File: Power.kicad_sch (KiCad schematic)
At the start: 25 parts, among them IC1 NJU7223DL1-33-TE1, J1 USB_C_Receptacle_USB2.0_14P, J2 SM02B-SRSS-TB_LF__SN_, U2 TPS2113APW, U3 MCP73831-2ACI_MC, U4 TPS61093DSKR

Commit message: Create PCB
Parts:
- removed IC1: NJU7223DL1-33-TE1, Footprints:TO-252-3-L1, symbol NJU7223DL1-33-TE1:NJU7223DL1-33-TE1
- removed J1: USB_C_Receptacle_USB2.0_14P, Connector_USB:USB_C_Receptacle_G-Switch_GT-USB-7010ASV, symbol Connector:USB_C_Receptacle_USB2.0_14P
- removed R4: 5.1K, Resistor_SMD:R_0603_1608Metric, symbol Device:R_Small
- removed R6: 200K, Resistor_SMD:R_0603_1608Metric, symbol Device:R_Small
- added C9: 1uF, Capacitor_SMD:C_0603_1608Metric, symbol Device:C_Small
- added J1: 2171790001, Footprints:MOLEX_2171790001, symbol 2171790001:2171790001
- added R2: 5.1K, Resistor_SMD:R_0402_1005Metric, symbol Device:R_Small
- added R7, R8: 100K, Resistor_SMD:R_0402_1005Metric, symbol Device:R_Small
- added U4: TLV1117LV33DCYR, Footprints:VREG_TLV1117LV33DCYR, symbol TLV1117LV33DCYR:TLV1117LV33DCYR
- C10: renamed from C8; footprint Capacitor_SMD:C_0603_1608Metric -> Capacitor_SMD:C_0805_2012Metric; DigiKey_Part_Number (none) -> 1276-1244-1-ND; Manufacturer_Part_Number (none) -> CL21A475KAQNNNE; Price (none) -> €0.30
- C11: renamed from C9; DigiKey_Part_Number (none) -> 311-1445-1-ND; Manufacturer_Part_Number (none) -> CC0603KRX5R8BB105; Price (none) -> €0.95
- C12: renamed from C10; DigiKey_Part_Number (none) -> 311-1341-1-ND; Manufacturer_Part_Number (none) -> CC0603KRX7R8BB104; Price (none) -> €0.48
- C13: renamed from C12; DigiKey_Part_Number (none) -> 311-1341-1-ND; Manufacturer_Part_Number (none) -> CC0603KRX7R8BB104; Price (none) -> €0.48
- C14: renamed from C13; DigiKey_Part_Number (none) -> 311-1445-1-ND; Manufacturer_Part_Number (none) -> CC0603KRX5R8BB105; Price (none) -> €0.95
- C4, C5, C7: DigiKey_Part_Number (none) -> 311-1341-1-ND; Manufacturer_Part_Number (none) -> CC0603KRX7R8BB104; Price (none) -> €0.48
- C6: footprint Capacitor_SMD:C_0603_1608Metric -> Capacitor_SMD:C_0805_2012Metric; DigiKey_Part_Number (none) -> 1276-6455-1-ND; Manufacturer_Part_Number (none) -> CL21A106KOQNNNG; Price (none) -> €0.16
- C8: renamed from C11; footprint Capacitor_SMD:C_0603_1608Metric -> Capacitor_SMD:C_0805_2012Metric; DigiKey_Part_Number (none) -> 1276-6455-1-ND; Manufacturer_Part_Number (none) -> CL21A106KOQNNNG; Price (none) -> €0.16
- J2: AVAILABILITY Good -> (none); Availability In Stock -> (none); Check_prices https://www.snapeda.com/parts/SM02B-SRSS-TB(LF)(SN)/JST/vie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 -> (none); DESCRIPTION SH Series 2 Position 1 mm Pitch Surface Mount Side Entry Sh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 -> (none); Description_1 Connector Header Surface Mount, Right Angle 2 position 0.03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 -> (none); DigiKey_Part_Number (none) -> 455-SM02B-SRSS-TBCT-ND; MF JST Sales -> (none); MP SM02B-SRSS-TB(LF)(SN) -> (none); Manufacturer_Part_Number (none) -> SM02B-SRSS-TB; PACKAGE None -> (none); PRICE 0.23 USD -> (none); Package None -> (none); Price None -> €0.37; SnapEDA_Link https://www.snapeda.com/parts/SM02B-SRSS-TB(LF)(SN)/JST/vie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 -> (none)
- L1: value 10uM -> 10uH; footprint Inductor_SMD:L_0603_1608Metric -> Inductor_SMD:L_0805_2012Metric; DigiKey_Part_Number (none) -> 587-2045-1-ND; Manufacturer_Part_Number (none) -> LBR2012T100K; Price (none) -> €0.10
- R10: renamed from R9; value 10.2K -> 10K; footprint Resistor_SMD:R_0603_1608Metric -> Resistor_SMD:R_0402_1005Metric; DigiKey_Part_Number (none) -> 311-10KJRCT-ND; Manufacturer_Part_Number (none) -> RC0402JR-0710KL; Price (none) -> €0.30
- R3: renamed from R2; value 10k -> 10K; footprint Resistor_SMD:R_0603_1608Metric -> Resistor_SMD:R_0402_1005Metric; DigiKey_Part_Number (none) -> 311-10KJRCT-ND; Manufacturer_Part_Number (none) -> RC0402JR-0710KL; Price (none) -> €0.30
- R4: renamed from R3; value 1k -> 1K; footprint Resistor_SMD:R_0603_1608Metric -> Resistor_SMD:R_1206_3216Metric; DigiKey_Part_Number (none) -> RNCP1206FTD1K00CT-ND; Manufacturer_Part_Number (none) -> RNCP1206FTD1K00; Price (none) -> €0.70
- R5: footprint Resistor_SMD:R_0603_1608Metric -> Resistor_SMD:R_0402_1005Metric; DigiKey_Part_Number (none) -> P5.1KDCCT-ND; Manufacturer_Part_Number (none) -> ERA-2AEB512X; Price (none) -> €0.20
- R6: renamed from R7; value 2k -> 2.7K; footprint Resistor_SMD:R_0603_1608Metric -> Resistor_SMD:R_1206_3216Metric; DigiKey_Part_Number (none) -> 311-2.70KFRCT-ND; Manufacturer_Part_Number (none) -> RC1206FR-072K7L; Price (none) -> €0.10
- R9: renamed from R8; value 294K -> 330K; footprint Resistor_SMD:R_0603_1608Metric -> Resistor_SMD:R_1206_3216Metric; DigiKey_Part_Number (none) -> A129840CT-ND; Manufacturer_Part_Number (none) -> CRGCQ1206F330K; Price (none) -> €0.10
- U2: Availability In Stock -> (none); Check_prices https://www.snapeda.com/parts/TPS2113APW/Texas+Instruments/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 -> (none); Description_1 2.8-V to 5.5-V, 84-mΩ, 1.25-A, power mux with automatic swi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 -> (none); DigiKey_Part_Number (none) -> 296-34596-5-ND; MF Texas Instruments -> (none); MP TPS2113APW -> (none); Manufacturer_Part_Number (none) -> TPS2113APW; Package TSSOP-8 Texas Instruments -> (none); Price None -> €2.61; SnapEDA_Link https://www.snapeda.com/parts/TPS2113APW/Texas+Instruments/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 -> (none)
- U3: Availability In Stock -> (none); Check_prices https://www.snapeda.com/parts/MCP73831-2ACI/MC/Microchip/vi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 -> (none); Description_1 Charge Controller Li-Ion/Li-Pol 15mA to 500mA 4.2V 8-Pin DF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 -> (none); DigiKey_Part_Number (none) -> MCP73831-2ACI/MC-ND; MANUFACTURER MICROCHIP -> (none); MF Microchip -> (none); MP MCP73831-2ACI/MC -> (none); Manufacturer_Part_Number (none) -> MCP73831-2ACI/MC; PARTREV G -> (none); Package VFDFN-8 Microchip -> (none); Price None -> €0.75; STANDARD IPC 7351B -> (none); SnapEDA_Link https://www.snapeda.com/parts/MCP73831-2ACI/MC/Microchip/vi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 -> (none)
- U5: renamed from U4; Availability In Stock -> (none); Check_prices https://www.snapeda.com/parts/TPS61093DSKR/Texas+Instrument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 -> (none); Description_1 Low Input, 20V/1.1A Step-Up DC/DC Converter with Integrated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 -> (none); DigiKey_Part_Number (none) -> 296-39430-1-ND; MF Texas Instruments -> (none); MP TPS61093DSKR -> (none); Manufacturer_Part_Number (none) -> TPS61093DSKR; Package WSON-10 Texas Instruments -> (none); Price None -> €1.96; SnapEDA_Link https://www.snapeda.com/parts/TPS61093DSKR/Texas+Instrument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 -> (none)
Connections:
- net 3V3: now also C9.2
- net GND: now also R5.1, J1.A1B12 (GND1), J1.B1A12 (GND2), J1.SH1 (SHIELD1), J1.SH2 (SHIELD2), J1.SH3 (SHIELD3), J1.SH4 (SHIELD4), R2.2, R8.1, U4.1 (GND); no longer R5.2
- net USB_5V: now also J1.A4B9 (VBUS1), J1.B4A9 (VBUS2)
- net at C11.2, U5.6 (SS): now also R7.2
- net at U2.7 (OUT): now also U4.3 (IN)
- net 15V renamed 17V
- new net: R7.1, R8.2
- new net: C9.1, U4.2 (OUT_2)
- new net: J1.A5 (CC1), R2.1
- new net: J1.B5 (CC2), R5.2
- new net USB_N: J1.A7 (DN1), J1.B7 (DN2)
- new net USB_P: J1.A6 (DP1), J1.B6 (DP2)
- no-connect marks 3 -> 6
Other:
- moved on the sheet: C10, C11, C12, C13, C14, C5, J2, L1, R10, R9, U5

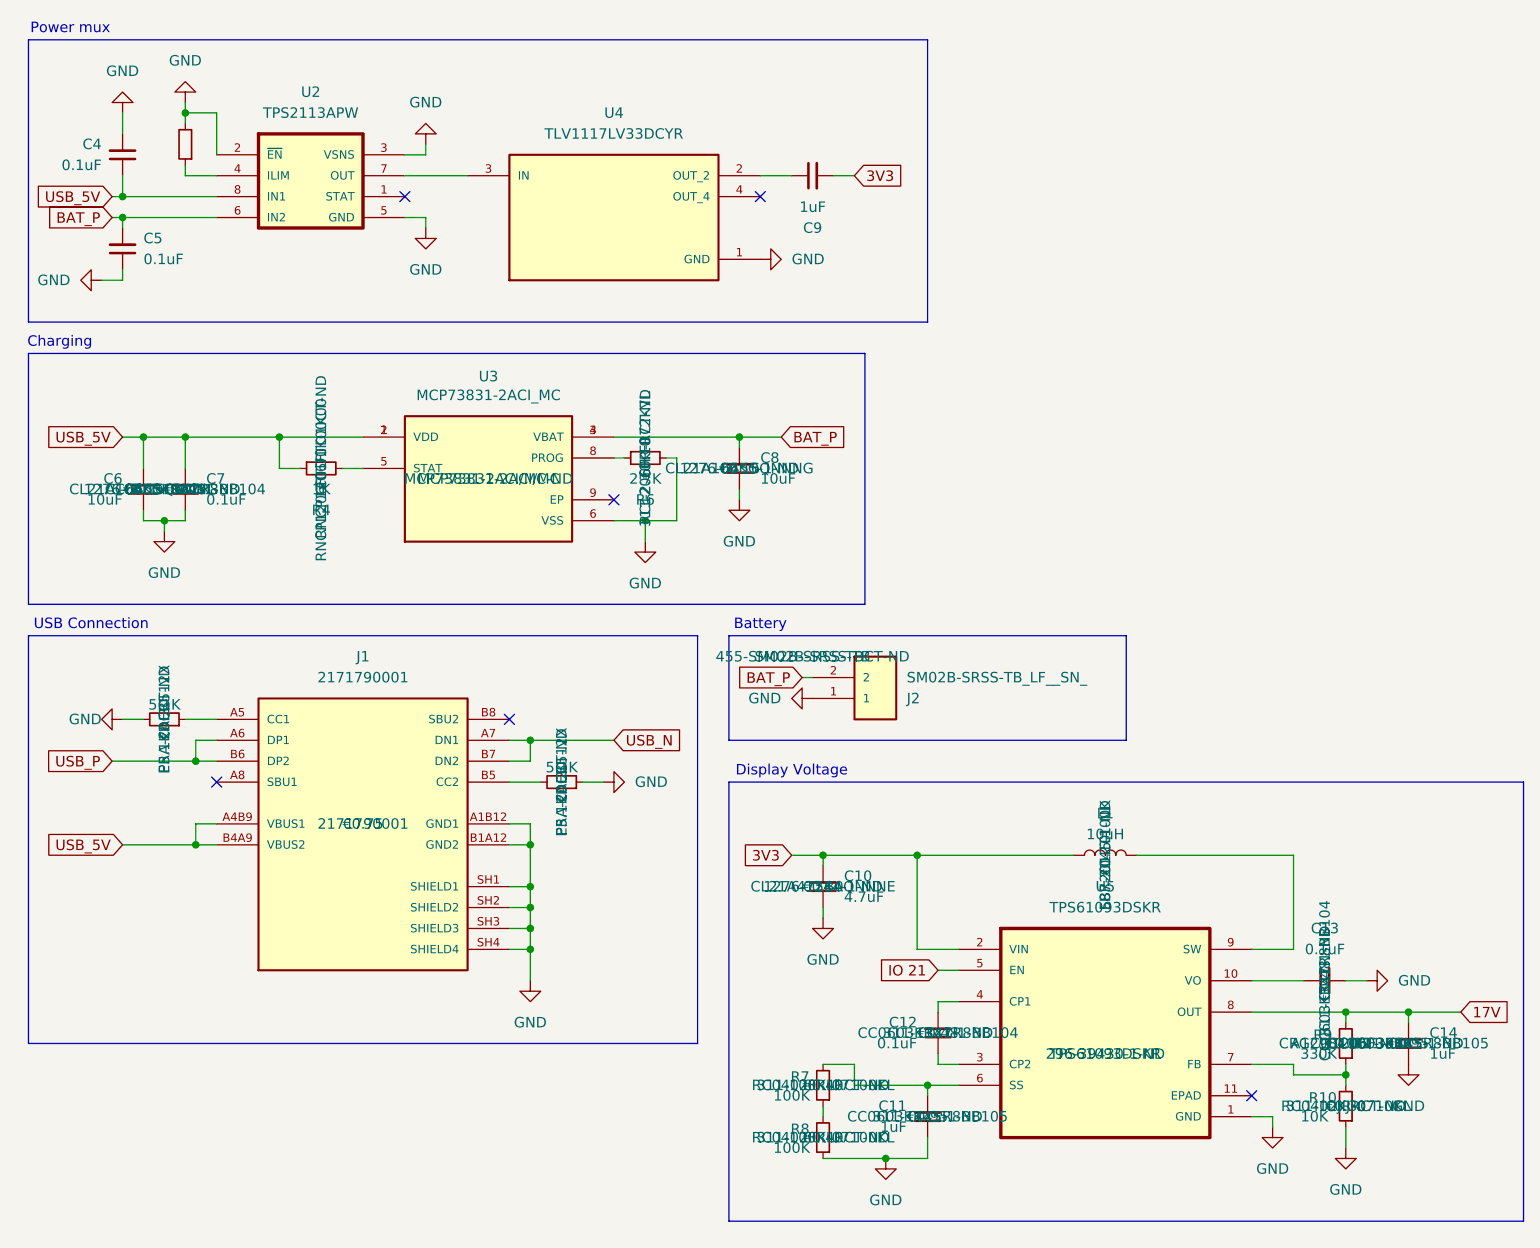
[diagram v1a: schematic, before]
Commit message: Fix minor design mistakes
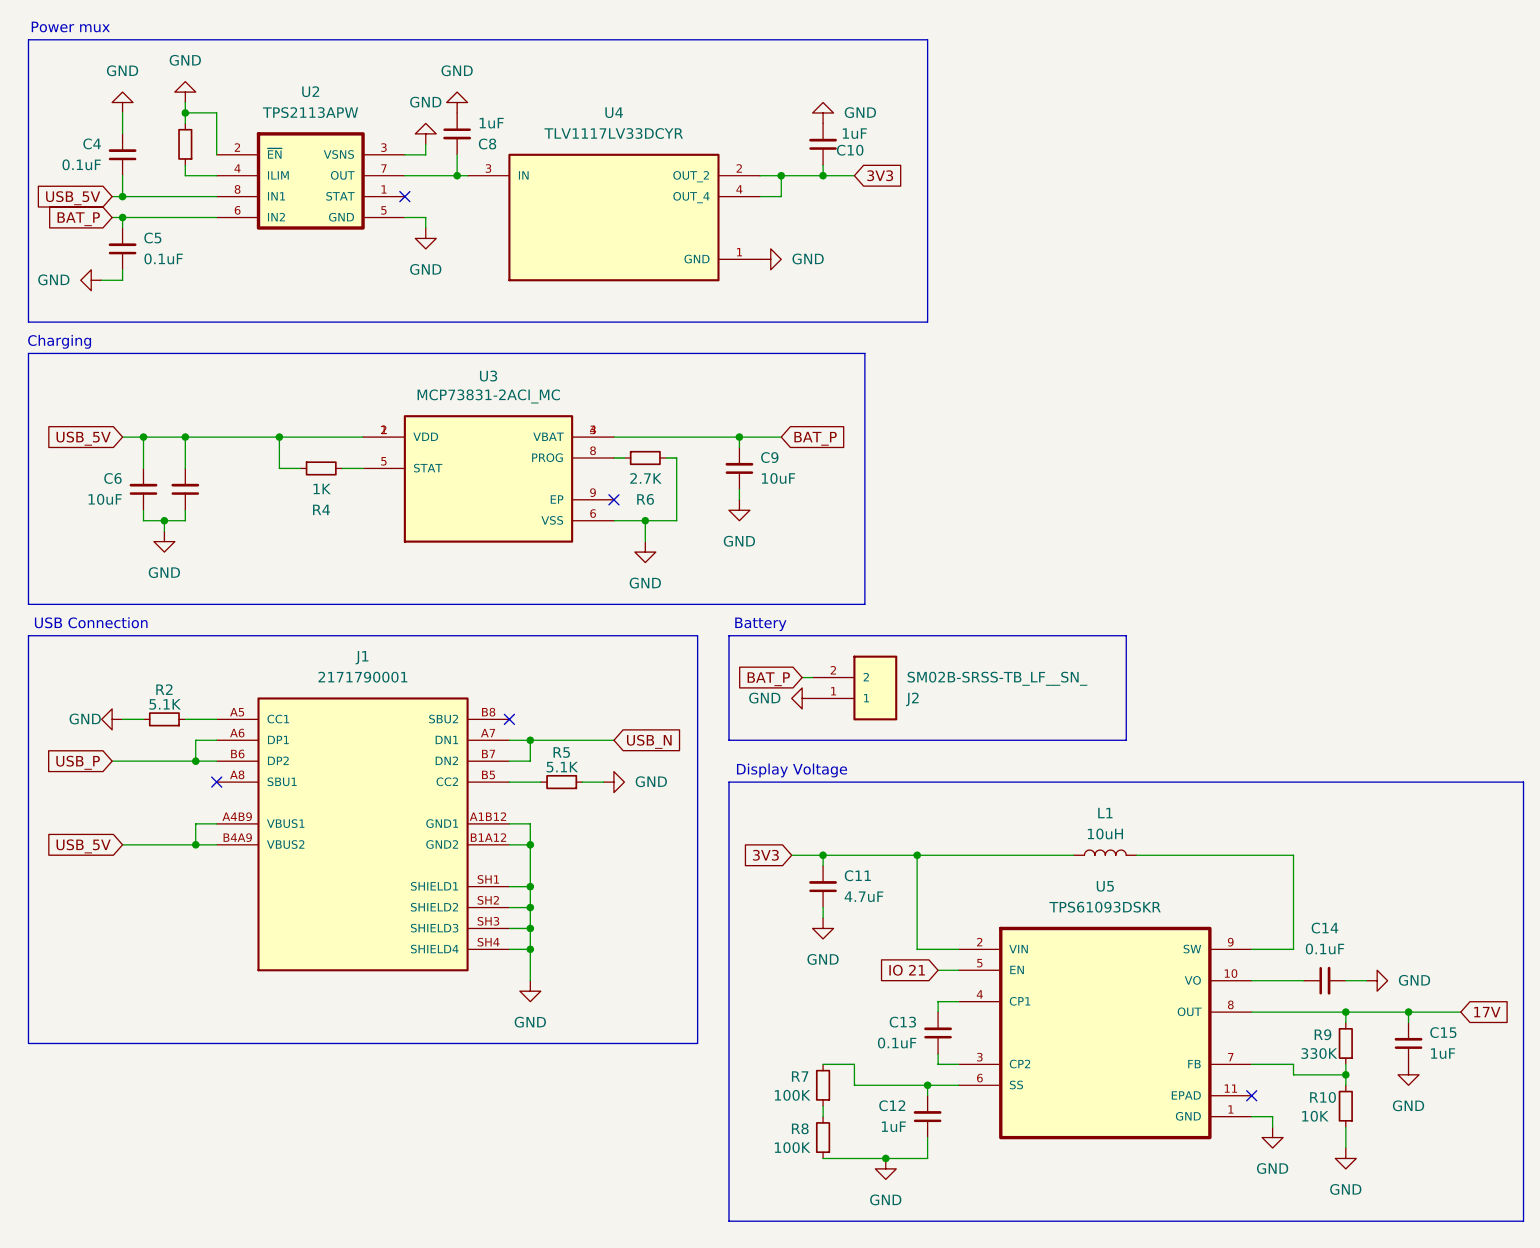
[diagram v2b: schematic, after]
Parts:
- added C8: 1uF, Capacitor_SMD:C_0603_1608Metric, symbol Device:C_Small
- renumbered C9 to C10, C10 to C11, C11 to C12, C12 to C13, C13 to C14, C14 to C15, C8 to C9
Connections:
- net 3V3: now also C10.1, U4.2 (OUT_2), U4.4 (OUT_4); no longer C10.2
- net GND: now also C10.2, C8.1
- net at U2.7 (OUT), U4.3 (IN): now also C8.2
- no-connect marks 6 -> 5
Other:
- moved on the sheet: C10
